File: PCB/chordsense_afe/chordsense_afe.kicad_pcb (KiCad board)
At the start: 2 copper layers, 25 parts, among them IC1 MCP6002-I_P, IC2 MCP6002-I_P, J1 ACJS-MHDR, J2 ACJS-MHDR, J3 Conn_01x08, J4 SJ3-35053B, U2 MCP3201

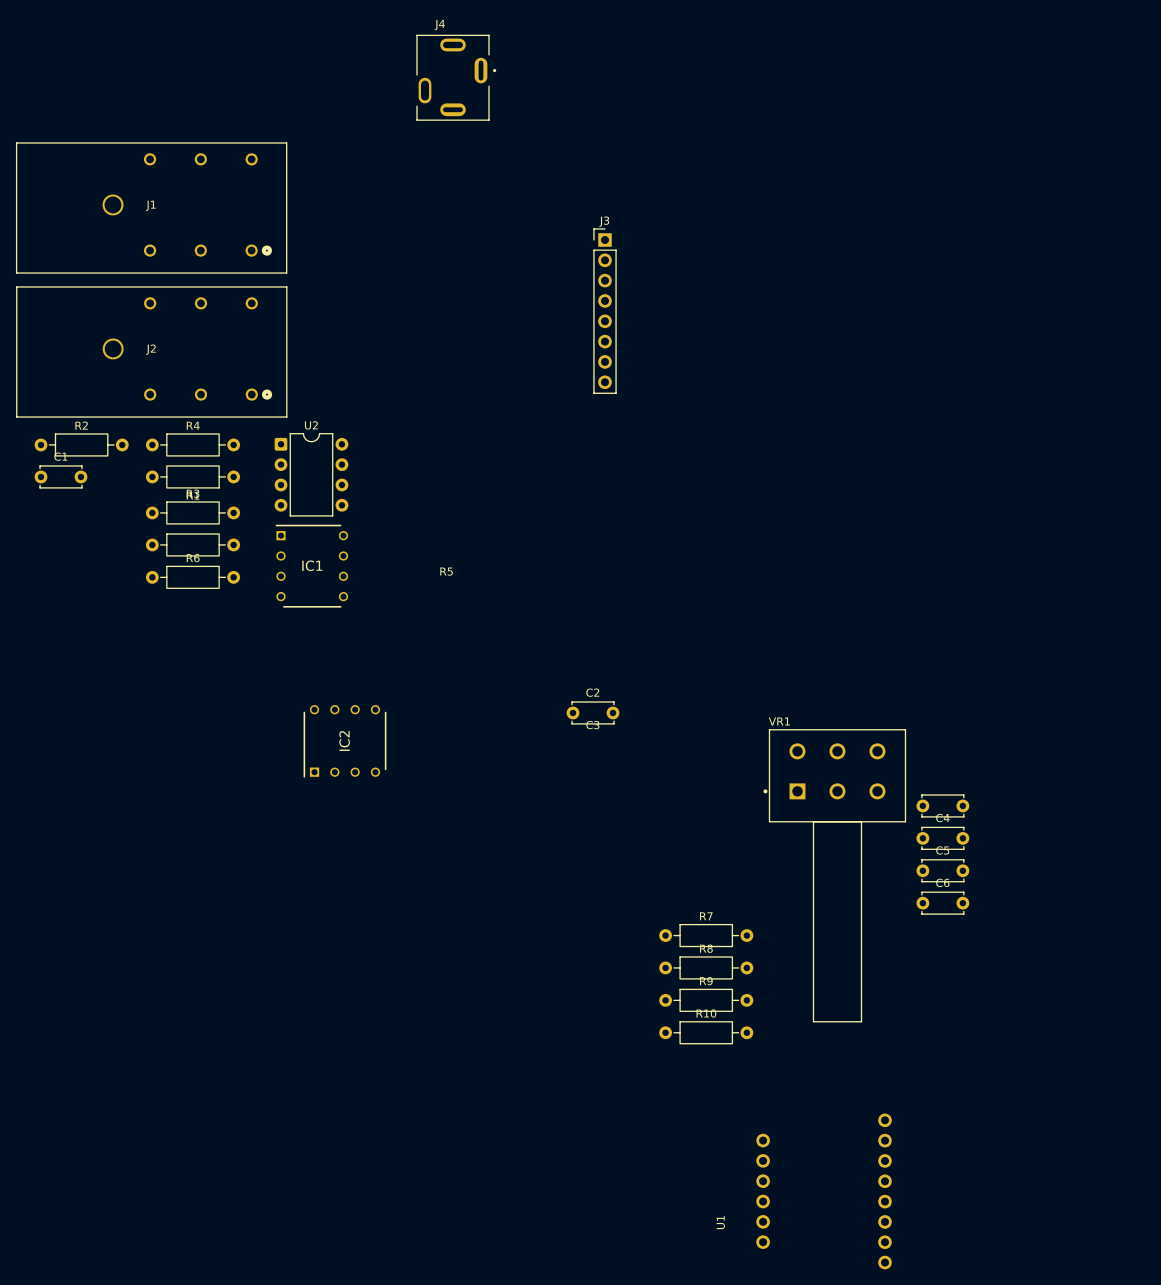
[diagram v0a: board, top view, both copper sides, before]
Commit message: initial PCB finished, ready to order remaining parts
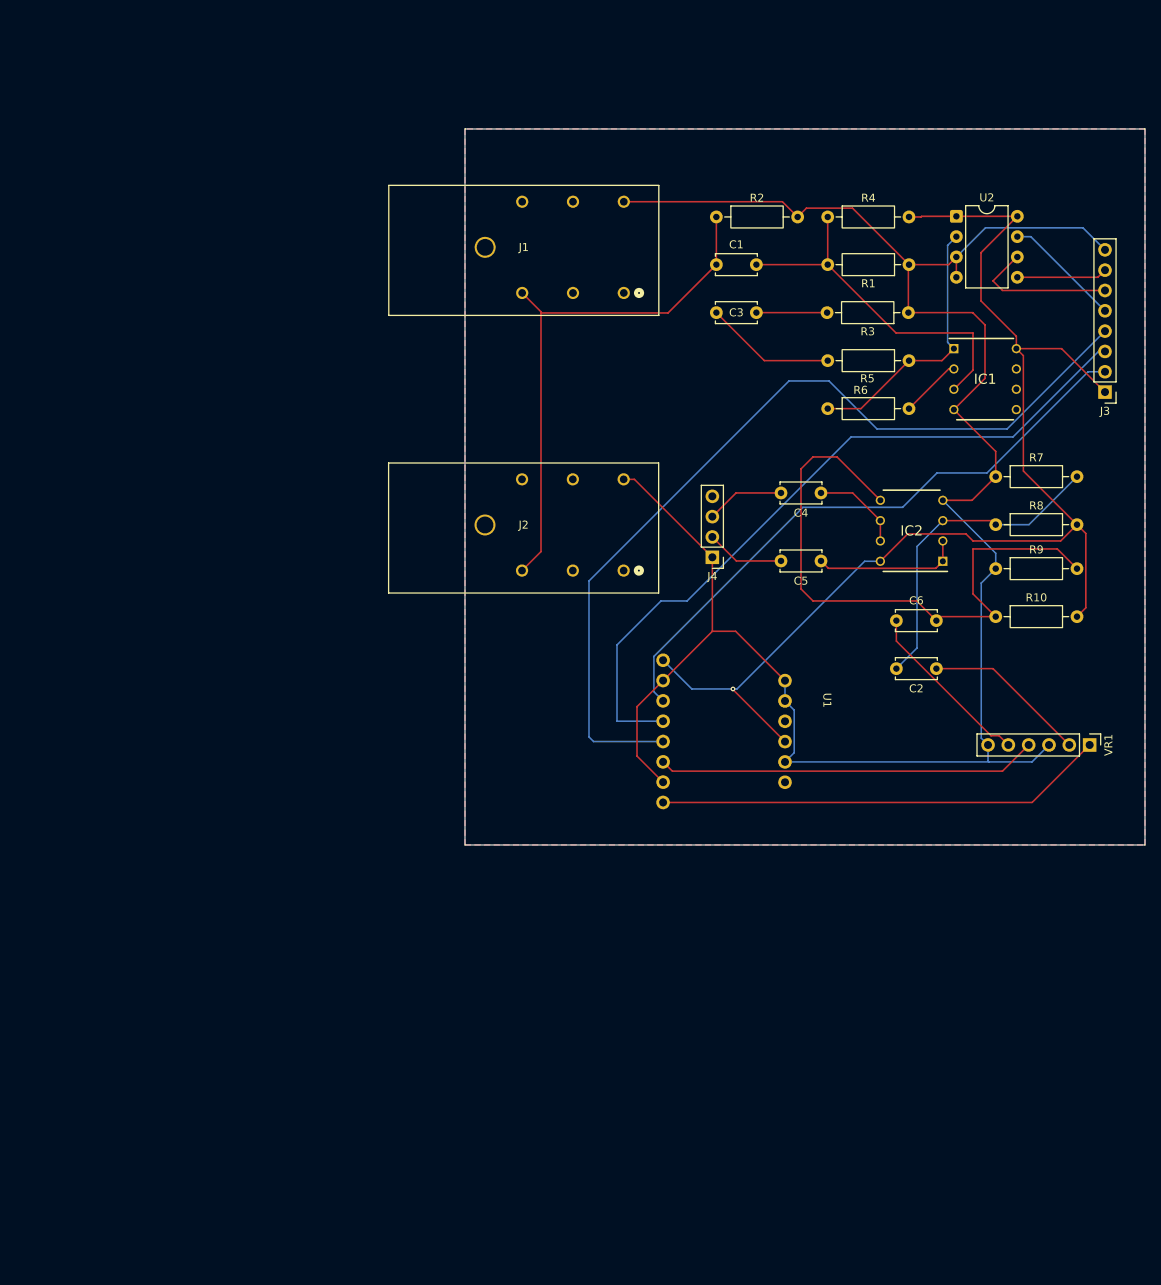
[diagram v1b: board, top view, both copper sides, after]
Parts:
- J4: footprint SJ3-35053B:SAMESKY_SJ3-35053B -> Connector_PinHeader_2.54mm:PinHeader_1x04_P2.54mm_Vertical
- VR1: footprint PDB182-K425K-103A:Bourns-PDB182-K425K-103A-0 -> Connector_PinHeader_2.54mm:PinHeader_1x06_P2.54mm_Vertical
- moved R3 97.8 mm to (127.4, 51.5), turned to 180 degrees
- moved R5 97.3 mm to (127.5, 57.5), turned to 180 degrees
- moved R2 89.1 mm to (103.4, 39.5)
- moved R4 89.1 mm to (117.3, 39.5)
- moved U2 89.1 mm to (133.4, 39.4)
- moved C1 88.5 mm to (103.4, 45.5)
- moved R1 88.5 mm to (127.5, 45.5)
- moved IC1 87.3 mm to (137.0, 59.8)
- moved R6 87.0 mm to (117.3, 63.5)
- moved IC2 75.5 mm to (127.8, 78.7), turned to 180 degrees
- moved R7 70.7 mm to (138.3, 72.0)
- moved R8 69.1 mm to (138.3, 78.0)
- moved R9 67.9 mm to (138.3, 83.5)
- moved J4 67.4 mm to (102.9, 82.0), turned to 180 degrees
- moved C3 66.9 mm to (103.4, 51.5)
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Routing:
- net GND: track 0.00 -> 258.4 mm
- net +3.3V: track 0.00 -> 156.4 mm, vias 0 -> 1
- net /PI_BCK: track 0.00 -> 111.4 mm
- net /PI_Din: track 0.00 -> 91.5 mm
- net Net-(IC2-VINB+): track 0.00 -> 77.6 mm
- net /PI_wsel: track 0.00 -> 77.2 mm
- net Net-(C1-Pad1): track 0.00 -> 67.0 mm
- net Net-(U1-Rout): track 0.00 -> 56.3 mm
- net Net-(U1-Lout): track 0.00 -> 47.5 mm
- net Net-(IC1-VINA+): track 0.00 -> 44.6 mm
- net Net-(IC2-VINA+): track 0.00 -> 40.4 mm
- net Net-(IC1-VOUTA): track 0.00 -> 33.7 mm
- net Net-(VR1B-R2_2): track 0.00 -> 21.9 mm
- net Net-(VR1A-R1_2): track 0.00 -> 20.6 mm
- net /PI_Dout: track 0.00 -> 19.4 mm
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- added copper zone on B.Cu, net GND
- added copper zone on F.Cu, net GND
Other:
- board outline added: 85 x 89.5 mm

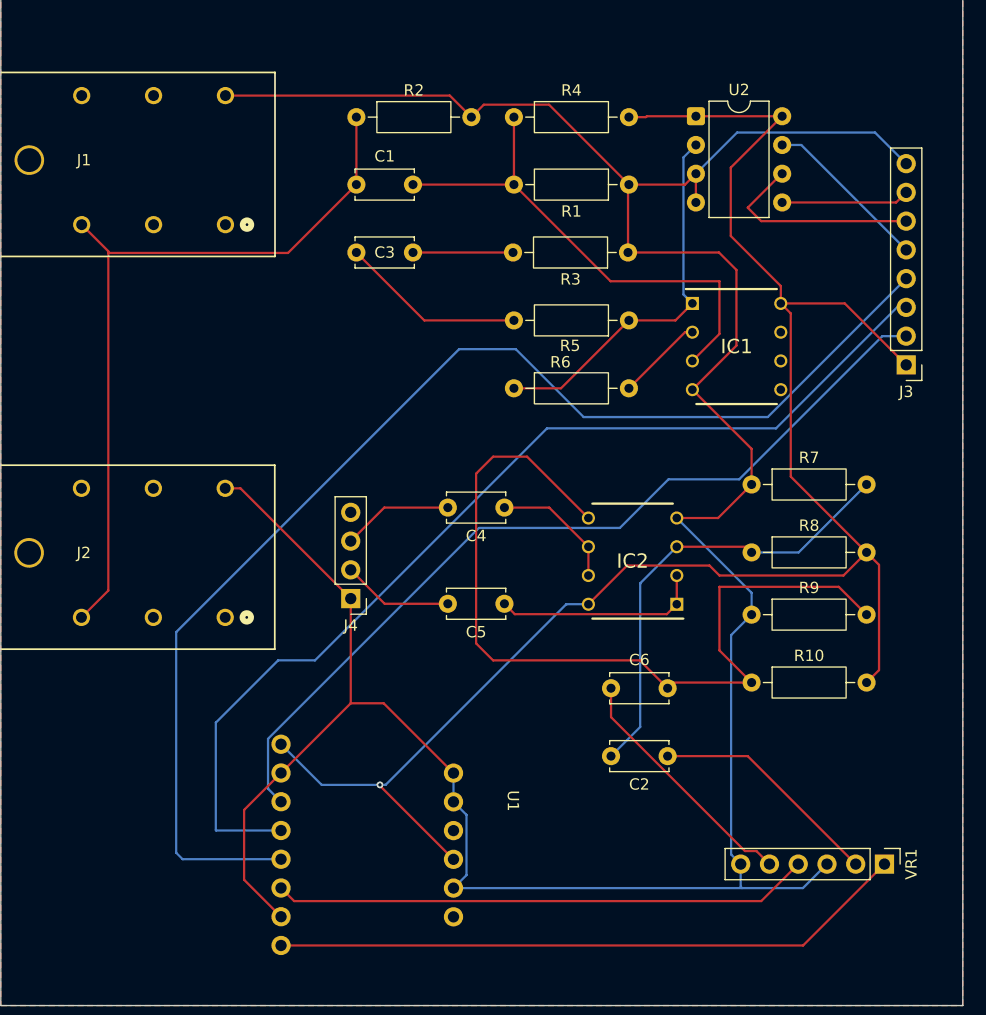
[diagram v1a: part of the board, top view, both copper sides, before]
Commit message: pcb fixes (wider holds for acjs)
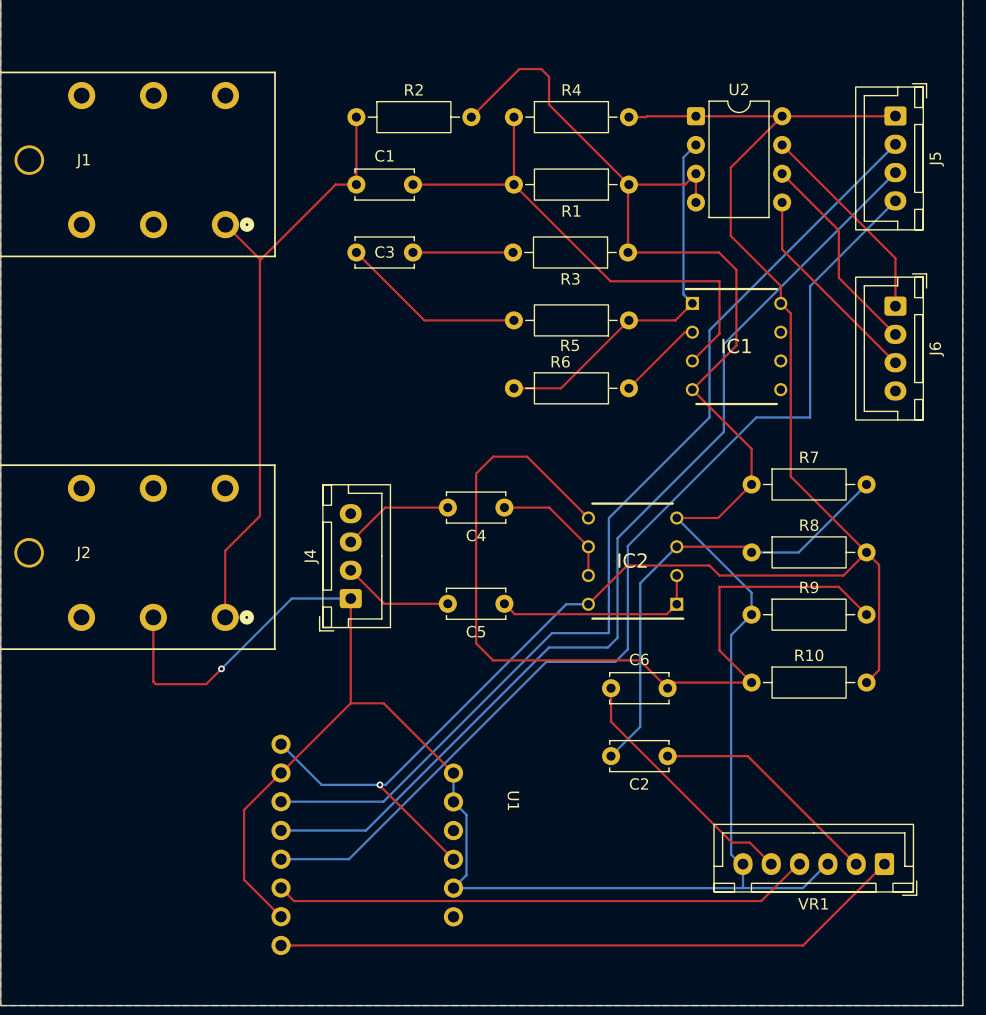
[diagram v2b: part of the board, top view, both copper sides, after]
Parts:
- removed J3: Conn_01x08, Connector_PinHeader_2.54mm:PinHeader_1x08_P2.54mm_Vertical
- added J5: Conn_01x04, Connector_JST:JST_XH_B4B-XH-A_1x04_P2.50mm_Vertical, F.Cu at (151.1, 39.4)
- added J6: Conn_01x04, Connector_JST:JST_XH_B4B-XH-A_1x04_P2.50mm_Vertical, F.Cu at (151.1, 56.2)
- J4: footprint Connector_PinHeader_2.54mm:PinHeader_1x04_P2.54mm_Vertical -> Connector_JST:JST_XH_B4B-XH-A_1x04_P2.50mm_Vertical
- VR1: footprint Connector_PinHeader_2.54mm:PinHeader_1x06_P2.54mm_Vertical -> Connector_JST:JST_XH_B6B-XH-A_1x06_P2.50mm_Vertical
- turned J4 to 90 degrees
- turned VR1 to 180 degrees
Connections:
- J1 pad 1: unconnected-(J1-Pad1) -> Net-(C1-Pad1)
- J1 pad 2: unconnected-(J1-Pad2) -> GND
- J1 pad 3: Net-(C1-Pad1) -> unconnected-(J1-Pad3)
- J1 pad 4: GND -> unconnected-(J1-Pad4)
- J2 pad 1: unconnected-(J2-Pad1) -> Net-(C1-Pad1)
- J2 pad 2: unconnected-(J2-Pad2) -> GND
- J2 pad 3: Net-(C1-Pad1) -> unconnected-(J2-Pad3)
- J2 pad 4: GND -> unconnected-(J2-Pad4)
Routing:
- net GND: track 258.4 -> 230.1 mm, vias 0 -> 1
- net /PI_BCK: track 111.4 -> 90.5 mm
- net Net-(C1-Pad1): track 67.0 -> 54.4 mm
- net /PI_wsel: track 77.2 -> 88.8 mm
- net /PI_CS: track 12.0 -> 18.3 mm
- net /PI_Din: track 91.5 -> 88.1 mm
- net +3.3V: track 156.4 -> 153.1 mm
- net /PI_CLK: track 15.5 -> 18.4 mm
- net /PI_Dout: track 19.4 -> 18.3 mm
